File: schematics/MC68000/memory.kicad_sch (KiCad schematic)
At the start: 0 parts

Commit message: cleanup zips and added memory map equations for pld
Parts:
- added J1: Conn_02x37_Row_Letter_Last, Connector_PinHeader_2.54mm:PinHeader_2x37_P2.54mm_Vertical, symbol Connector_Generic:Conn_02x37_Row_Letter_Last
- added R21: 10k, Resistor_THT:R_Axial_DIN0204_L3.6mm_D1.6mm_P5.08mm_Horizontal, symbol Device:R
- added U13: ROM_LOW, Package_DIP:DIP-28_W15.24mm, symbol Memory_EPROM:2764
- added U14: ROM_HIGH, Package_DIP:DIP-28_W15.24mm, symbol Memory_EPROM:2764
- added U15: RAM_LOW, Package_DIP:DIP-32_W15.24mm, symbol Memory_RAM:AS6C4008-55PCN
- added U16: RAM_HIGH, Package_DIP:DIP-32_W15.24mm, symbol Memory_RAM:AS6C4008-55PCN
- added U17: GAL20V8, symbol Logic_Programmable:PAL20L8
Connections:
- new net: R21.2, U13.27 (~{PGM}), U14.27 (~{PGM})
- new net +12: J1.23b (Pin_23b)
- new net +5V: J1.18a (Pin_18a), J1.18b (Pin_18b)
- new net -5: J1.27b (Pin_27b)
- new net GND: J1.17a (Pin_17a), J1.17b (Pin_17b)
- new net IRQ1: J1.6b (Pin_6b)
- new net IRQ2: J1.7b (Pin_7b)
- new net IRQ3: J1.8b (Pin_8b)
- new net IRQ4: J1.9b (Pin_9b)
- new net IRQ5: J1.10b (Pin_10b)
- new net IRQ6: J1.11b (Pin_11b)
- new net IRQ7: J1.12b (Pin_12b)
- new net bA1: J1.1a (Pin_1a), U13.10 (A0), U14.10 (A0), U15.12 (A0), U16.12 (A0)
- new net bA10: J1.10a (Pin_10a), U13.24 (A9), U14.24 (A9), U15.26 (A9), U16.26 (A9)
- new net bA11: J1.11a (Pin_11a), U13.21 (A10), U14.21 (A10), U15.23 (A10), U16.23 (A10)
- new net bA12: J1.12a (Pin_12a), U13.23 (A11), U14.23 (A11), U15.25 (A11), U16.25 (A11)
- new net bA13: J1.13a (Pin_13a), U13.2 (A12), U14.2 (A12), U15.4 (A12), U16.4 (A12), U17.1 (I1)
- new net bA14: J1.14a (Pin_14a), U15.28 (A13), U16.28 (A13), U17.2 (I2)
- new net bA15: J1.15a (Pin_15a), U15.3 (A14), U16.3 (A14), U17.3 (I3)
- new net bA16: J1.16a (Pin_16a), U15.31 (A15), U16.31 (A15), U17.4 (I4)
- new net bA17: J1.19a (Pin_19a), U15.2 (A16), U16.2 (A16), U17.5 (I5)
- new net bA18: J1.20a (Pin_20a), U15.30 (A17), U16.30 (A17), U17.6 (I6)
- new net bA19: J1.21a (Pin_21a), U15.1 (A18), U16.1 (A18), U17.7 (I7)
- new net bA2: J1.2a (Pin_2a), U13.9 (A1), U14.9 (A1), U15.11 (A1), U16.11 (A1)
- new net bA20: J1.1b (Pin_1b), U17.8 (I8)
- new net bA21: J1.2b (Pin_2b)
- new net bA22: J1.3b (Pin_3b)
- new net bA23: J1.4b (Pin_4b)
- new net bA3: J1.3a (Pin_3a), U13.8 (A2), U14.8 (A2), U15.10 (A2), U16.10 (A2)
- new net bA4: J1.4a (Pin_4a), U13.7 (A3), U14.7 (A3), U15.9 (A3), U16.9 (A3)
- new net bA5: J1.5a (Pin_5a), U13.6 (A4), U14.6 (A4), U15.8 (A4), U16.8 (A4)
- new net bA6: J1.6a (Pin_6a), U13.5 (A5), U14.5 (A5), U15.7 (A5), U16.7 (A5)
- new net bA7: J1.7a (Pin_7a), U13.4 (A6), U14.4 (A6), U15.6 (A6), U16.6 (A6)
- new net bA8: J1.8a (Pin_8a), U13.3 (A7), U14.3 (A7), U15.5 (A7), U16.5 (A7)
- new net bA9: J1.9a (Pin_9a), U13.25 (A8), U14.25 (A8), U15.27 (A8), U16.27 (A8)
- new net bD0: J1.22a (Pin_22a), U13.11 (D0), U15.13 (DQ0)
- new net bD1: J1.23a (Pin_23a), U13.12 (D1), U15.14 (DQ1)
- new net bD10: J1.32a (Pin_32a), U14.13 (D2), U16.15 (DQ2)
- new net bD11: J1.33a (Pin_33a), U14.15 (D3), U16.17 (DQ3)
- new net bD12: J1.34a (Pin_34a), U14.16 (D4), U16.18 (DQ4)
- new net bD13: J1.35a (Pin_35a), U14.17 (D5), U16.19 (DQ5)
- new net bD14: J1.36a (Pin_36a), U14.18 (D6), U16.20 (DQ6)
- new net bD15: J1.37a (Pin_37a), U14.19 (D7), U16.21 (DQ7)
- new net bD2: J1.24a (Pin_24a), U13.13 (D2), U15.15 (DQ2)
- new net bD3: J1.25a (Pin_25a), U13.15 (D3), U15.17 (DQ3)
- new net bD4: J1.26a (Pin_26a), U13.16 (D4), U15.18 (DQ4)
- new net bD5: J1.27a (Pin_27a), U13.17 (D5), U15.19 (DQ5)
- new net bD6: J1.28a (Pin_28a), U13.18 (D6), U15.20 (DQ6)
- new net bD7: J1.29a (Pin_29a), U13.19 (D7), U15.21 (DQ7)
- new net bD8: J1.30a (Pin_30a), U14.11 (D0), U16.13 (DQ0)
- new net bD9: J1.31a (Pin_31a), U14.12 (D1), U16.14 (DQ1)
- new net bE: J1.19b (Pin_19b)
- new net bFC0: J1.20b (Pin_20b)
- new net bFC1: J1.21b (Pin_21b)
- new net bFC2: J1.22b (Pin_22b)
- new net /BERR: J1.25b (Pin_25b)
- new net /BG: J1.29b (Pin_29b)
- new net /BGACK: J1.31b (Pin_31b)
- new net /BR: J1.30b (Pin_30b)
- new net /DTACK: J1.28b (Pin_28b)
- new net /IO_CS: U17.21 (IO21)
- new net /RAM1_CS: U17.19 (IO19)
- new net /RAM2_CS: U15.22 (CE#), U16.22 (CE#), U17.18 (IO18)
- new net /RAM3_CS: U17.17 (IO17)
- new net /RAM4_CS: U17.20 (I020)
- new net /RAM_CS: J1.36b (Pin_36b)
- new net /ROM_CE: J1.37b (Pin_37b), U13.20 (~{CE}), U14.20 (~{CE}), U17.22 (IO22)
- new net /VPA: J1.26b (Pin_26b)
- new net /bAS: J1.13b (Pin_13b), U17.9 (I9)
- new net /bLDS: J1.15b (Pin_15b), U13.22 (~{OE}), U15.24 (OE#)
- new net /bR/W: J1.24b (Pin_24b), U15.29 (WE#), U16.29 (WE#)
- new net /bUDS: J1.14b (Pin_14b), U14.22 (~{OE}), U16.24 (OE#)
- new net /bVMA: J1.16b (Pin_16b)
- no-connect marks 0 -> 9
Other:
- note added: "; PINOS DE ENTRADA A13 PIN 1 ; Barramento de endereço A14 PIN 2 A15 PIN 3 A16 PIN 4 A17 PIN 5 A18 PIN 6 A19 PIN 7 A20 PIN 8 !AS PIN 9 ; Address Strobe ; PINOS DE SAÍDA !ROM_CS PIN 19 ; ROM (0x00000-0x01FFF) !IO_CS PIN 18 ; I/O (0x02000-0x03FFF) !RAM4_CS PIN 17 ; RAM1 (0x004000-0x07FFFF) !RAM1_CS PIN 16 ; RAM2 (0x080000-0x0FFFFF) !RAM2_CS PIN 16 ; RAM2 (0x100000-0x17FFFF) !RAM3_CS PIN 16 ; RAM2 (0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"
- note added: "MEMORY CARD 16KB ROM 1MB RAM"

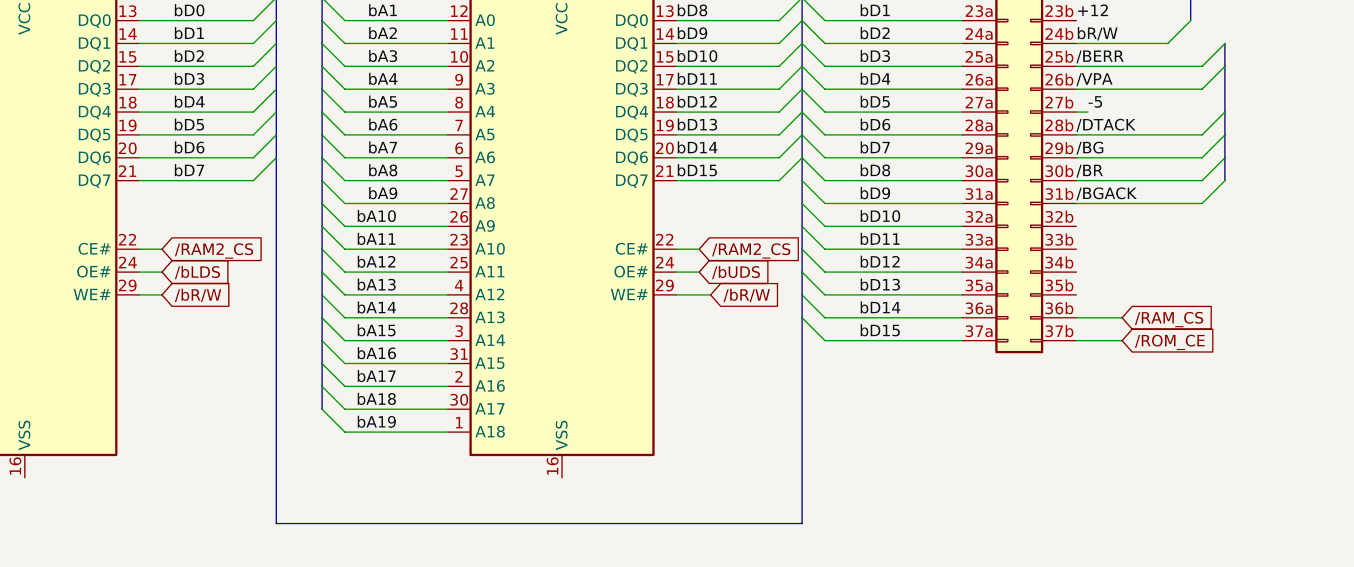
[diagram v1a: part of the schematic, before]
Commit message: added schemati for cpu without buffers
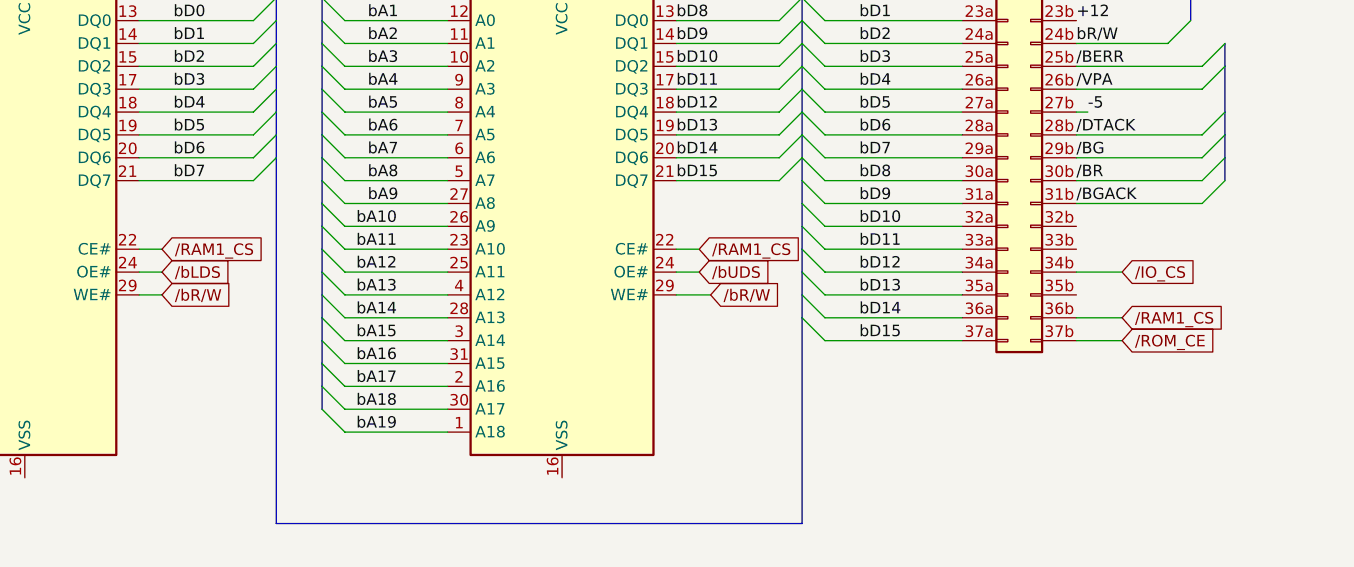
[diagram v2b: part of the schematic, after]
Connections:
- net /RAM_CS is gone; now on net /RAM1_CS: J1.36b (Pin_36b)
- net /IO_CS: now also J1.34b (Pin_34b)
- net /RAM1_CS: now also U15.22 (CE#), U16.22 (CE#)
- net /RAM2_CS: no longer U15.22 (CE#), U16.22 (CE#)
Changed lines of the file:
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@@
+    (stroke (width 0) (type default))
+  )
+  (wire (pts (xy 271.78 132.08) (xy 266.7 132.08))
     (stroke (width 0) (type default))
   )
@@
     (effects (font (size 1.27 1.27)) (justify left bottom))
   )
-  (label "{slash}bAS" (at 63.5 138.43 0)
+  (label "{slash}bAS" (at 63.5 138.43 0) (fields_autoplaced)
     (effects (font (size 1.27 1.27)) (justify left bottom))
   )
@@
     (effects (font (size 1.27 1.27)) (justify left bottom))
   )
-  (label "bA20" (at 63.5 135.89 0)
+  (label "bA20" (at 63.5 135.89 0) (fields_autoplaced)
     (effects (font (size 1.27 1.27)) (justify left bottom))
   )
@@
     )
   )
-  (global_label "{slash}RAM_CS" (shape input) (at 271.78 137.16 0) (fields_autoplaced)
-    (effects (font (size 1.27 1.27)) (justify left))
-    (property "Intersheetrefs" "${INTERSHEET_REFS}" (at 283.3528 137.16 0)
-      (effects (font (size 1.27 1.27)) (justify left) hide)
-    )
-  )
-  (global_label "{slash}RAM2_CS" (shape input) (at 165.1 129.54 0) (fields_autoplaced)
+  (global_label "{slash}RAM1_CS" (shape input) (at 271.78 137.16 0) (fields_autoplaced)
+    (effects (font (size 1.27 1.27)) (justify left))
+    (property "Intersheetrefs" "${INTERSHEET_REFS}" (at 284.5623 137.16 0)
+      (effects (font (size 1.27 1.27)) (justify left) hide)
+    )
+  )
+  (global_label "{slash}RAM1_CS" (shape input) (at 165.1 129.54 0) (fields_autoplaced)
     (effects (font (size 1.27 1.27)) (justify left))
     (property "Intersheetrefs" "${INTERSHEET_REFS}" (at 177.8823 129.54 0)
@@
     )
   )
-  (global_label "{slash}RAM2_CS" (shape input) (at 224.79 129.54 0) (fields_autoplaced)
+  (global_label "{slash}RAM1_CS" (shape input) (at 224.79 129.54 0) (fields_autoplaced)
     (effects (font (size 1.27 1.27)) (justify left))
     (property "Intersheetrefs" "${INTERSHEET_REFS}" (at 237.5723 129.54 0)
@@
     )
   )
+  (global_label "{slash}IO_CS" (shape input) (at 271.78 132.08 0) (fields_autoplaced)
+    (effects (font (size 1.27 1.27)) (justify left))
+    (property "Intersheetrefs" "${INTERSHEET_REFS}" (at 281.4781 132.08 0)
+      (effects (font (size 1.27 1.27)) (justify left) hide)
+    )
+  )

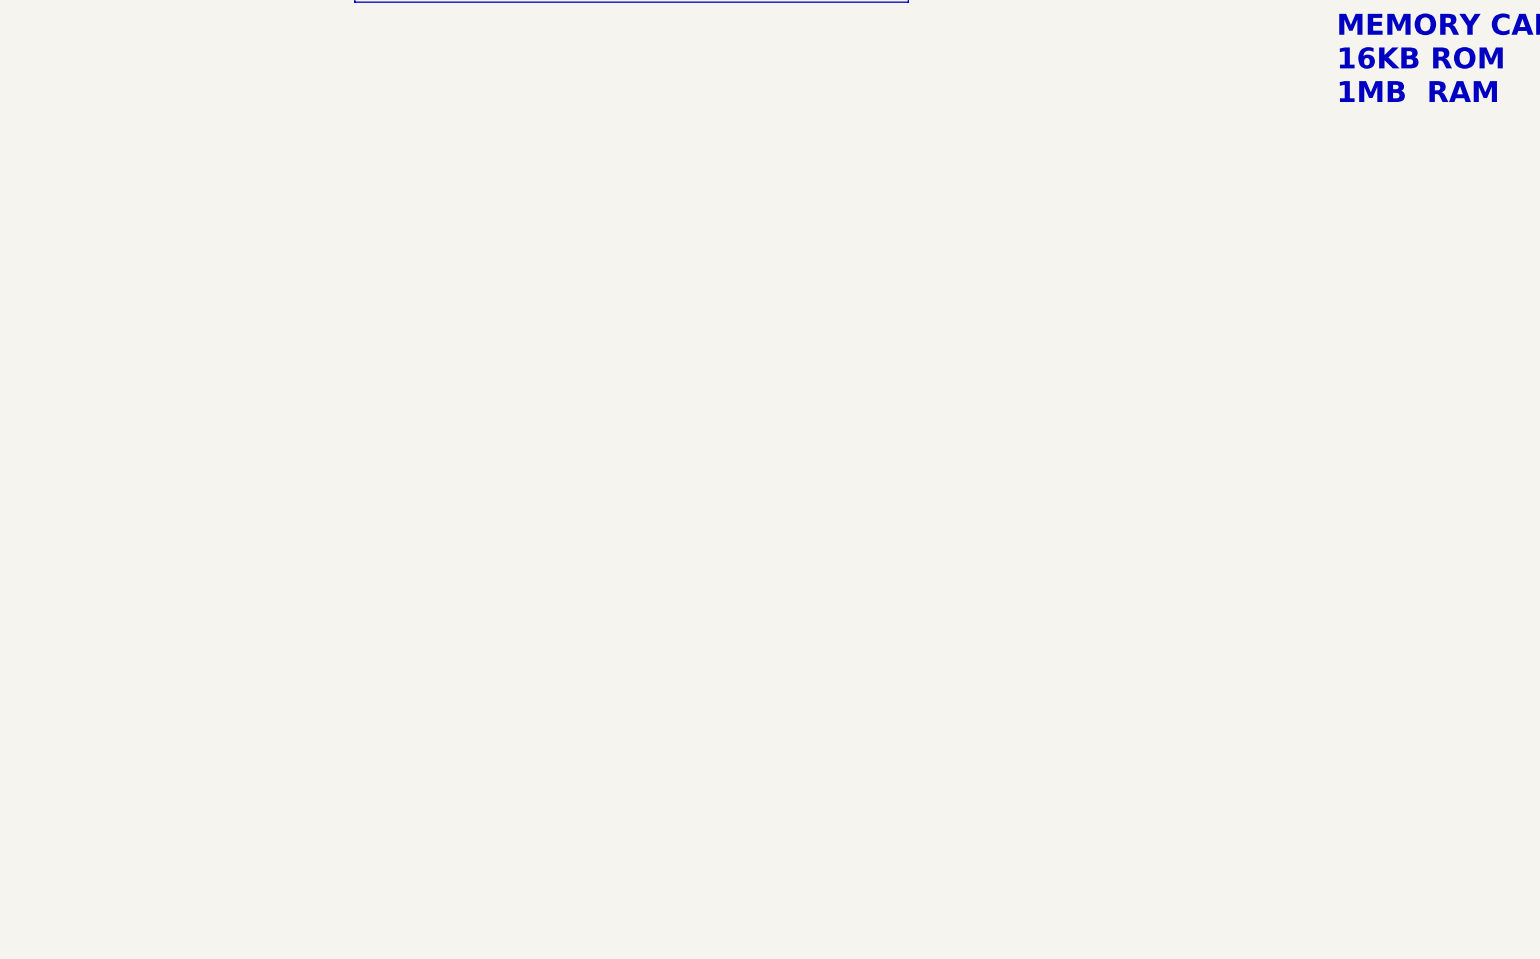
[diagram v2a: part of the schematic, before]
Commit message: Added test_led.asm
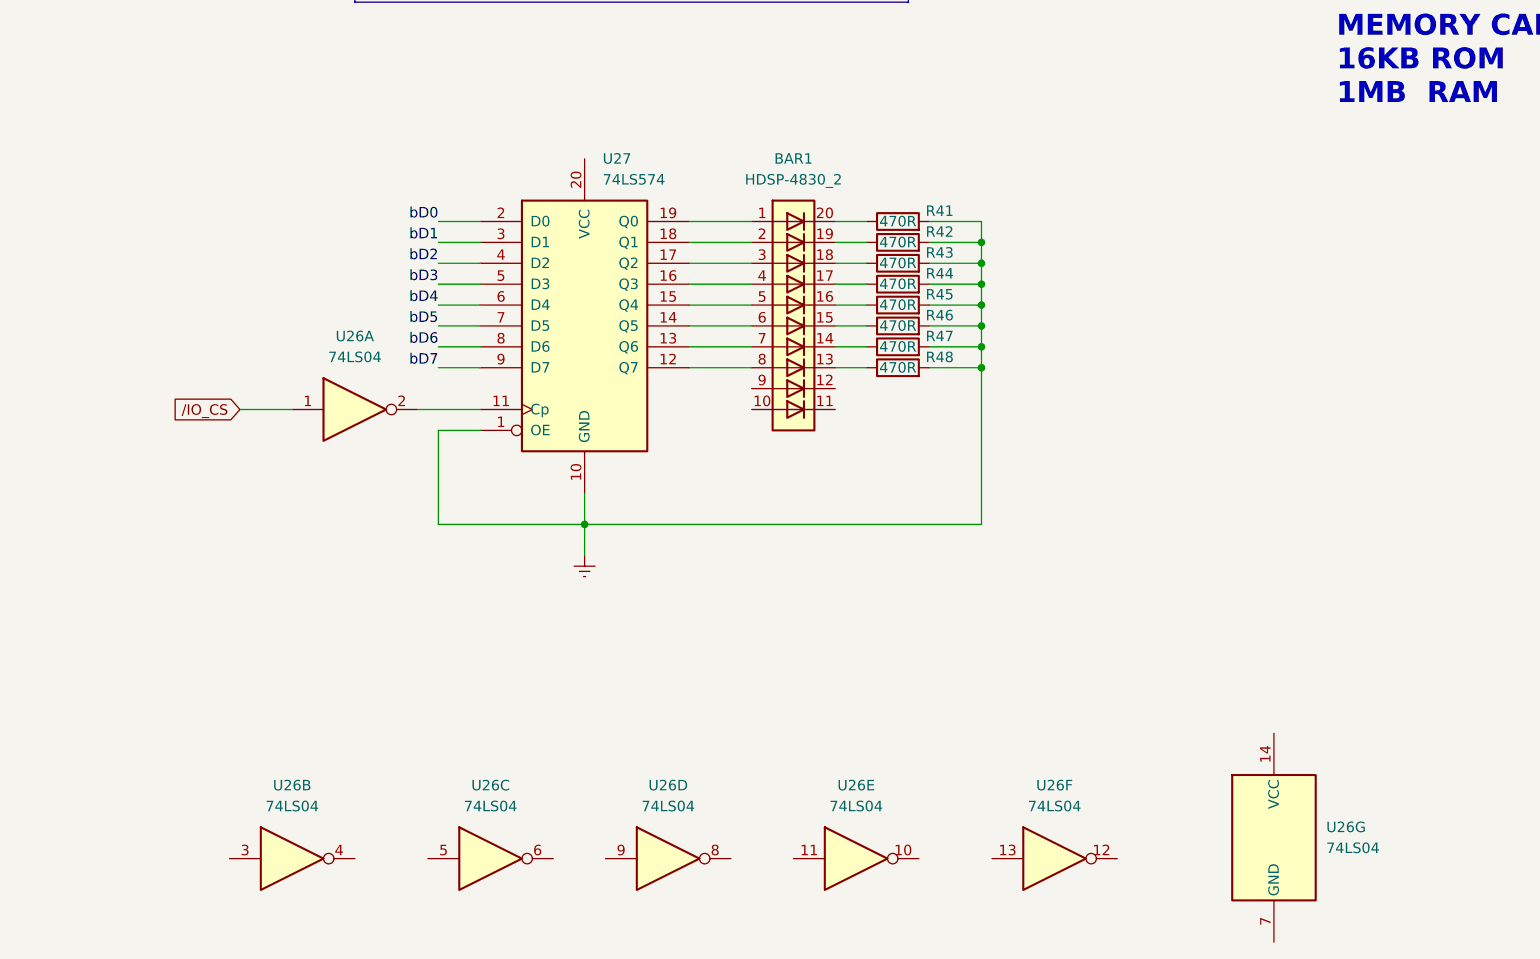
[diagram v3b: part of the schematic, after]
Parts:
- added BAR1: HDSP-4830_2, Display:HDSP-4830, symbol LED:HDSP-4830_2
- added R41, R42, R43, R44, R45, R46, R47, R48: 470R, symbol Device:R
- added U26: 74LS04, symbol 74xx:74LS04
- added U27: 74LS574, symbol 74xx:74LS574
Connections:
- net bD0: now also U27.2 (D0)
- net bD1: now also U27.3 (D1)
- net bD2: now also U27.4 (D2)
- net bD3: now also U27.5 (D3)
- net bD4: now also U27.6 (D4)
- net bD5: now also U27.7 (D5)
- net bD6: now also U27.8 (D6)
- net bD7: now also U27.9 (D7)
- net /IO_CS: now also U26.1
- new net: BAR1.17 (K), R44.1
- new net: BAR1.18 (K), R43.1
- new net: BAR1.13 (K), R48.1
- new net: BAR1.19 (K), R42.1
- new net: BAR1.20 (K), R41.1
- new net: U26.2, U27.11 (Cp)
- new net: BAR1.8 (A), U27.12 (Q7)
- new net: BAR1.7 (A), U27.13 (Q6)
- new net: BAR1.6 (A), U27.14 (Q5)
- new net: BAR1.5 (A), U27.15 (Q4)
- new net: BAR1.4 (A), U27.16 (Q3)
- new net: BAR1.3 (A), U27.17 (Q2)
- new net: BAR1.2 (A), U27.18 (Q1)
- new net: BAR1.1 (A), U27.19 (Q0)
- new net: BAR1.16 (K), R45.1
- new net: BAR1.15 (K), R46.1
- new net: BAR1.14 (K), R47.1
- new net GNDREF: R41.2, R42.2, R43.2, R44.2, R45.2, R46.2, R47.2, R48.2, U27.1 (OE), U27.10 (GND)
